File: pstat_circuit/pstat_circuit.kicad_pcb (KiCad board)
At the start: 2 copper layers, 53.3 x 124.5 mm, 40 parts, among them P1 LMP91000-2, P2 LMP91000-2, P3 LMP91000-2, P4 LMP91000-2, P5 LMP91000-2, P6 PWR_BUS, P7 PSTAT_CTRL, P8 I2C_BUS, U1 MCP1700-2, U2 CD4051BM96-2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

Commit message: Finish first draft of PSTAT pcb
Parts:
- moved P6 12.7 mm to (121.9, 129.5)
- moved P7 7.62 mm to (121.9, 142.2)
- moved R7 3.81 mm to (101.6, 141.5)
- moved U2 3.81 mm to (104.1, 146.3)
- moved C5 2.81 mm to (112.8, 151.4)
- moved C8 1.52 mm to (114.6, 133.9)
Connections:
- P7 pad 1: /PSEL0 -> /MENB
- P7 pad 2: /PSEL1 -> /PSEL2
- P7 pad 3: /PSEL2 -> /PSEL1
- P7 pad 4: /MENB -> /PSEL0
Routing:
- net /PSEL0: track 32.4 -> 48.8 mm
- net +3V3: track 380.0 -> 394.7 mm, vias 6 -> 8
- net /MENB: track 4.93 -> 17.0 mm, vias 0 -> 1
- net /PSEL1: track 35.9 -> 46.3 mm
- net /PSEL2: track 40.6 -> 48.3 mm
- net GND: track 126.2 -> 130.4 mm, vias 13 -> 14
- net Net-(P4-Pad2): track 54.6 -> 50.5 mm
- net Net-(P5-Pad2): track 92.6 -> 96.5 mm
- net Net-(P1-Pad2): track 96.4 -> 92.8 mm
- net Net-(P3-Pad2): track 146.4 -> 149.8 mm
- net Net-(P2-Pad2): track 138.4 -> 135.1 mm
- added copper zone on B.Cu, net GND
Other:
- board text added: "0"
- board text added: "1"
- board text added: "2"
- board text added: "3V3"
- board text added: "GND"
- board text added: "M"
- board text added: "S0"
- board text added: "S1"
- board text added: "S2"
- board text added: "S3"
- board text added: "S4"
- board text added: "SCL"
- board text added: "SDA"

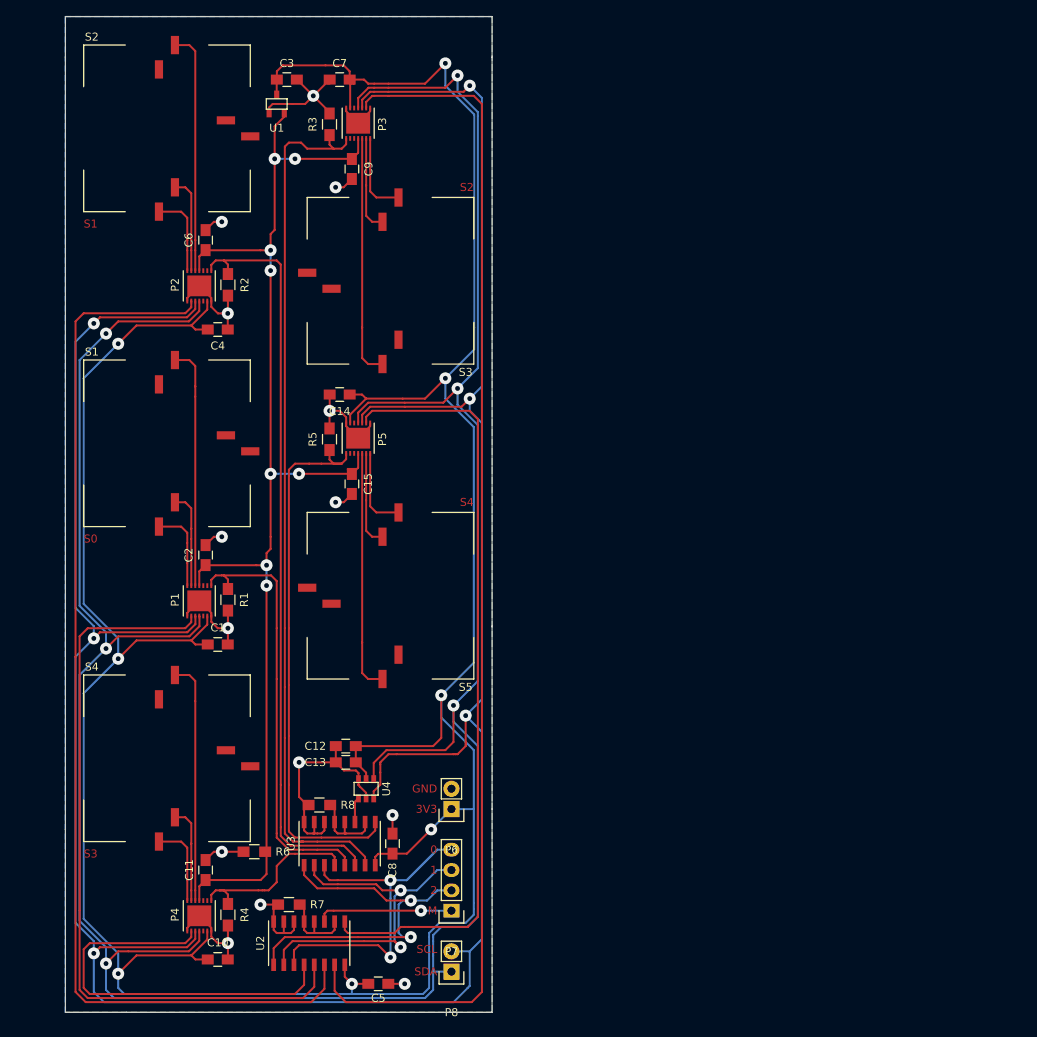
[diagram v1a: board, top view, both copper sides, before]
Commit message: Rotate PCB design
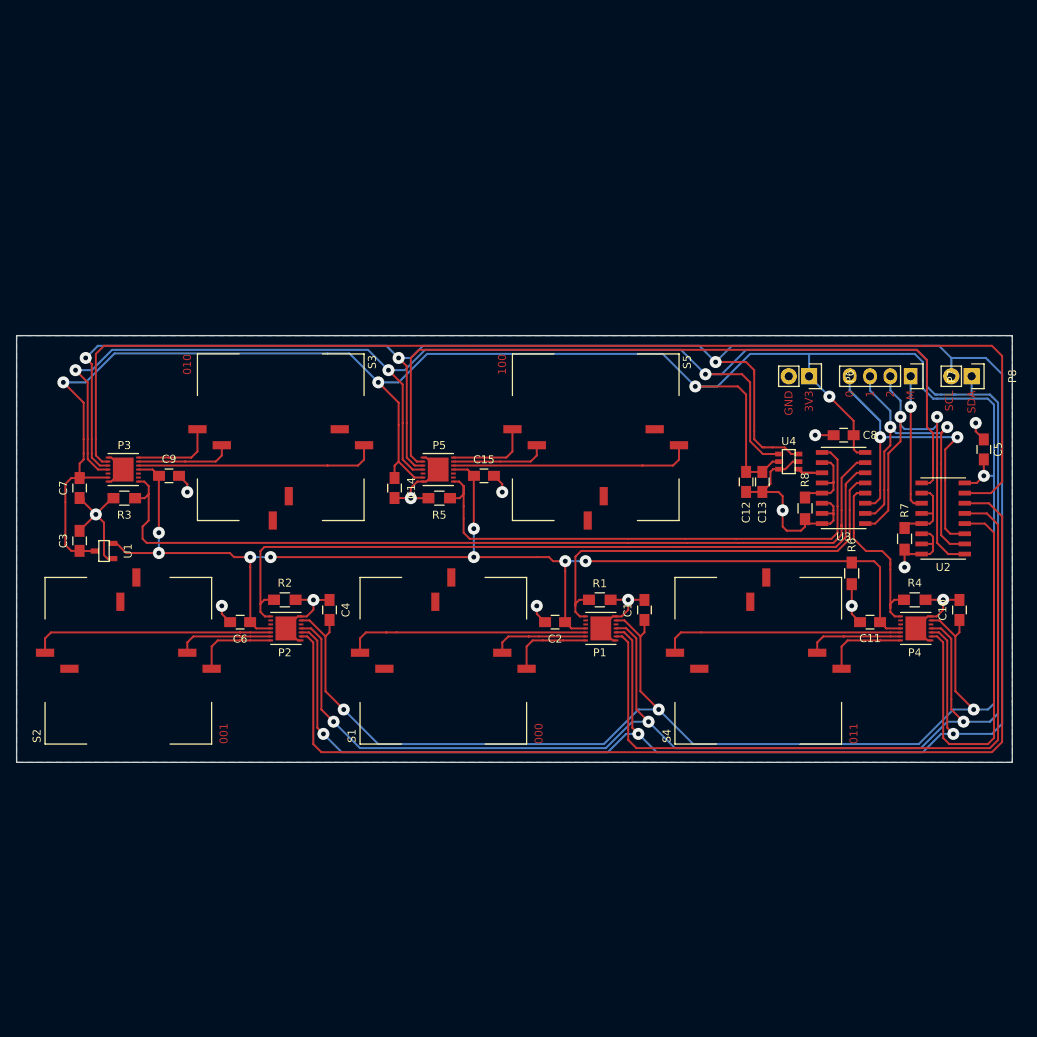
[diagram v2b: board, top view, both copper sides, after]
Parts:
- moved C10 102.5 mm to (185.4, 104.6), turned to 90 degrees
- moved C5 101.0 mm to (188.5, 84.6), turned to 90 degrees
- moved P4 99.8 mm to (181.9, 108.5), turned to 180 degrees
- moved P8 98.8 mm to (186.9, 75.4), turned to 270 degrees
- moved U2 95.4 mm to (183.4, 93.2), turned to 270 degrees
- moved R4 94.4 mm to (179.8, 103.4), turned to 0 degrees
- moved R7 89.5 mm to (178.6, 95.8), turned to 90 degrees
- moved C11 88.7 mm to (174.2, 106.2), turned to 180 degrees
- moved P7 88.1 mm to (179.3, 75.4), turned to 270 degrees
- moved R6 82.4 mm to (172.0, 100.1), turned to 90 degrees
- moved U3 77.1 mm to (170.9, 89.4), turned to 270 degrees
- moved C8 76.1 mm to (170.9, 82.8), turned to 180 degrees
- moved S4 74.9 mm to (160.3, 111.0), turned to 270 degrees
- moved R8 71.1 mm to (166.1, 91.9), turned to 90 degrees
- moved P6 70.2 mm to (166.6, 75.4), turned to 270 degrees
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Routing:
- net GND: track 130.4 -> 131.2 mm
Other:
- board size 53.3 x 124.5 mm -> 124.5 x 53.3 mm
- board text added: "000"
- board text added: "001"
- board text added: "010"
- board text added: "011"
- board text added: "100"
- board text removed: "S0"
- board text removed: "S1"
- board text removed: "S2"
- board text removed: "S3"
- board text removed: "S4"
